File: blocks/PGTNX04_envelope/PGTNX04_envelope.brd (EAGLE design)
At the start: 45.6 x 67.3 mm, 72 parts, among them IC1 TL084P, IC2 AS3310

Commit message: Committed a load of changes
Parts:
- added STN2: HEADER/MALE/01, connectors:HEADER/MALE/01
- moved +V3 26.7 mm to (25.4, 68.6), turned to 270 degrees
- moved GND2 25.7 mm to (22.9, 68.6), turned to 270 degrees
- moved -V3 25.2 mm to (20.3, 68.6), turned to 270 degrees
- moved +V2 23.3 mm to (25.4, 66.0), turned to 270 degrees
- moved GND3 22.2 mm to (22.9, 66.0), turned to 270 degrees
- moved -V2 21.6 mm to (20.3, 66.0), turned to 270 degrees
- moved +V 20.1 mm to (25.4, 63.5), turned to 270 degrees
- moved GND 18.8 mm to (22.9, 63.5), turned to 270 degrees
- moved -V 18.1 mm to (20.3, 63.5), turned to 270 degrees
- moved C1 15.9 mm to (31.8, 64.8), turned to 90 degrees
- moved C2 12.7 mm to (14.0, 64.8)
- moved U$5 9.92 mm to (10.2, 57.1)
- moved U$3 2.54 mm to (3.81, 66.0)
- moved U$4 2.54 mm to (41.9, 66.0)
- moved STN3 2.54 mm to (44.5, 19.1)
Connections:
- new net N$32: STN2.1
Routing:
- net N$8: track 54.2 -> 10.6 mm
- net -12V: track 114.4 -> 82.5 mm, vias 0 -> 1
- net N$20: track 42.3 -> 13.9 mm
- net +12V: track 129.9 -> 151.1 mm
- net N$22: track 22.4 -> 41.7 mm
- net N$30: track 22.7 -> 9.69 mm
- net N$23: track 40.3 -> 27.6 mm
- net N$17: track 47.6 -> 38.4 mm, vias 1 -> 0
- net N$27: track 23.1 -> 15.5 mm
- net N$4: track 20.3 -> 24.8 mm
- net N$10: track 22.0 -> 18.3 mm
- net N$9: track 13.4 -> 11.3 mm
- net N$19: track 11.2 -> 13.2 mm
- net N$21: track 15.1 -> 13.3 mm
- net N$28: track 19.9 -> 18.3 mm
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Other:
- board size 45.6 x 67.3 mm -> 45.6 x 69.8 mm
- board text added: "PGTN020B"
- board text added: "Rob Ellis 2020"

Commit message: Corrected resistor value
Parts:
- R12: value 150R -> 200k
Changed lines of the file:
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@@
 <?xml version="1.0" encoding="utf-8"?>
 <!DOCTYPE eagle SYSTEM "eagle.dtd">
-<eagle version="8.5.2">
+<eagle version="9.6.0">
 <drawing>
 <settings>
-<setting alwaysvectorfont="yes"/>
+<setting alwaysvectorfont="no"/>
 <setting keepoldvectorfont="yes"/>
 <setting verticaltext="up"/>
@@
 <param name="checkStop" value="0"/>
 <param name="checkValues" value="0"/>
+<param name="checkNames" value="1"/>
+<param name="checkWireStubs" value="1"/>
+<param name="checkPolygonWidth" value="0"/>
 <param name="useDiameter" value="13"/>
 <param name="maxErrors" value="50"/>
@@
 <attribute name="SPICEPREFIX" value="X" x="1.27" y="19.05" size="1.778" layer="27" display="off"/>
 </element>
-<element name="R12" library="resistors" package="RESISTOR/7.5" value="150R" x="7.62" y="21.59" smashed="yes">
+<element name="R12" library="resistors" package="RESISTOR/7.5" value="200k" x="7.62" y="21.59" smashed="yes">
 <attribute name="NAME" x="5.08" y="21.082" size="1.016" layer="25" ratio="10"/>
 <attribute name="VALUE" x="4.699" y="22.9362" size="1.27" layer="27" ratio="10"/>
@@
 <attribute name="SPICEPREFIX" value="X" x="44.45" y="19.05" size="1.778" layer="27" rot="R180" display="off"/>
 </element>
-<element name="U$1" library="mechanical" package="STANDOFF/3.0" value="" x="3.81" y="3.81"/>
-<element name="U$2" library="mechanical" package="STANDOFF/3.0" value="" x="41.91" y="3.81"/>
-<element name="U$3" library="mechanical" package="STANDOFF/3.0" value="" x="3.81" y="66.04"/>
-<element name="U$4" library="mechanical" package="STANDOFF/3.0" value="" x="41.91" y="66.04"/>
-<element name="U$5" library="mechanical" package="PIGATRON-LOGO" value="" x="10.16" y="57.15"/>
+<element name="U$1" library="mechanical" package="STANDOFF/3.0" value="" x="3.81" y="3.81" smashed="yes"/>
+<element name="U$2" library="mechanical" package="STANDOFF/3.0" value="" x="41.91" y="3.81" smashed="yes"/>
+<element name="U$3" library="mechanical" package="STANDOFF/3.0" value="" x="3.81" y="66.04" smashed="yes"/>
+<element name="U$4" library="mechanical" package="STANDOFF/3.0" value="" x="41.91" y="66.04" smashed="yes"/>
+<element name="U$5" library="mechanical" package="PIGATRON-LOGO" value="" x="10.16" y="57.15" smashed="yes"/>
 <element name="STN2" library="connectors" package="HEADER/MALE/01" value="HEADER/MALE/01" x="44.45" y="16.51" smashed="yes" rot="R180">
 <attribute name="NAME" x="42.545" y="16.764" size="1.016" layer="25" ratio="10" rot="R180"/>
@@
 </signal>
 </signals>
+<mfgpreviewcolors>
+<mfgpreviewcolor name="soldermaskcolor" color="0xC8008000"/>
+<mfgpreviewcolor name="silkscreencolor" color="0xFFFEFEFE"/>
+<mfgpreviewcolor name="backgroundcolor" color="0xFF282828"/>
+<mfgpreviewcolor name="coppercolor" color="0xFFFFBF00"/>
+<mfgpreviewcolor name="substratecolor" color="0xFF786E46"/>
+</mfgpreviewcolors>
 </board>
 </drawing>

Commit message: Changed resistor value
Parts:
- R1: value 750R -> 470R
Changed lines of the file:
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@@
 <?xml version="1.0" encoding="utf-8"?>
 <!DOCTYPE eagle SYSTEM "eagle.dtd">
-<eagle version="9.6.0">
+<eagle version="9.5.0">
 <drawing>
 <settings>
@@
 <attribute name="VALUE" x="35.179" y="44.704" size="1.27" layer="27" ratio="10" rot="R180"/>
 </element>
-<element name="R1" library="resistors" package="RESISTOR/7.5" value="750R" x="12.7" y="11.43" smashed="yes">
+<element name="R1" library="resistors" package="RESISTOR/7.5" value="470R" x="12.7" y="11.43" smashed="yes">
 <attribute name="NAME" x="10.16" y="10.922" size="1.016" layer="25" ratio="10"/>
 <attribute name="VALUE" x="9.779" y="12.7762" size="1.27" layer="27" ratio="10"/>

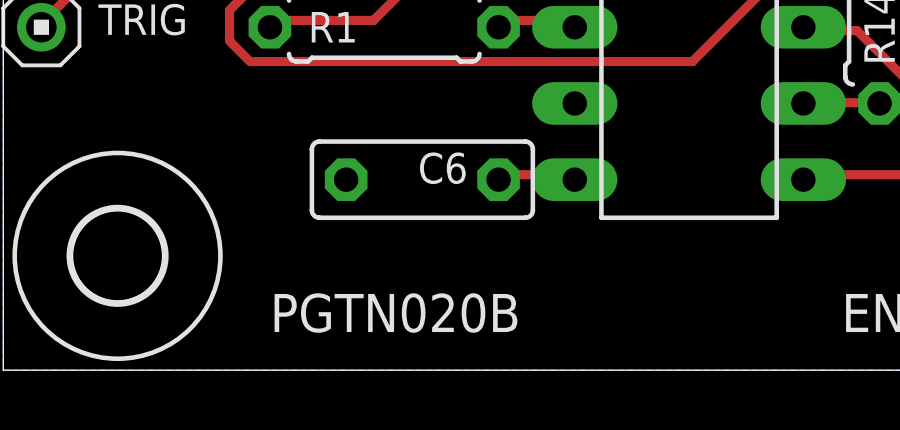
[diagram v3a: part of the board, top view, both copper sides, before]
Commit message: Connected C7 to ground
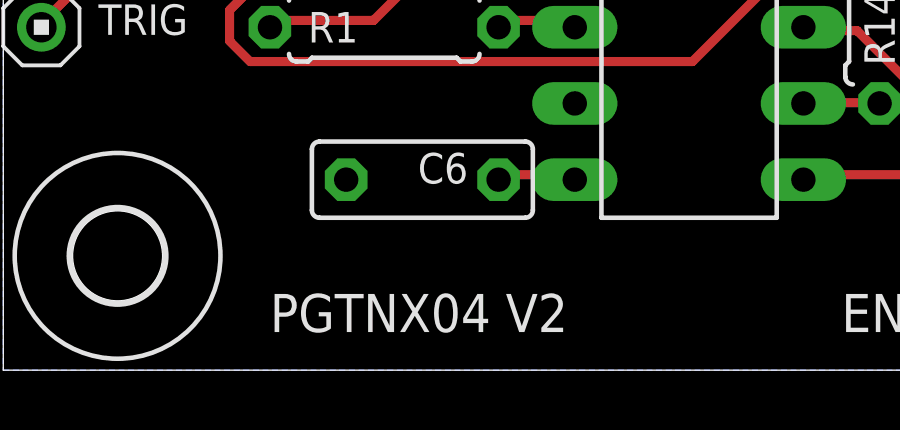
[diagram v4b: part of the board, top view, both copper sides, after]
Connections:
- removed net PE: C7.2
- net GND: now also C7.2
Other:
- board text added: "PGTNX04 V2"
- board text removed: "PGTN020B"
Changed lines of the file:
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@@
 <?xml version="1.0" encoding="utf-8"?>
 <!DOCTYPE eagle SYSTEM "eagle.dtd">
-<eagle version="9.5.0">
+<eagle version="9.6.0">
 <drawing>
 <settings>
@@
 <text x="27.94" y="1.27" size="1.27" layer="25">ENVELOPE</text>
 <dimension x1="0" y1="0" x2="0" y2="69.85" x3="-3.81" y3="34.925" textsize="1.016" layer="51"/>
-<text x="8.89" y="1.27" size="1.27" layer="25">PGTN020B</text>
+<text x="8.89" y="1.27" size="1.27" layer="25">PGTNX04 V2</text>
 <dimension x1="0" y1="0" x2="45.72" y2="0" x3="22.86" y3="-3.81" textsize="1.016" layer="51"/>
 <text x="1.27" y="50.8" size="1.27" layer="25">Rob Ellis 2020</text>
@@
 <contactref element="IC1" pad="10"/>
 <contactref element="IC1" pad="12"/>
+<contactref element="C7" pad="2"/>
 </signal>
 <signal name="+12V">
@@
 <wire x1="18.8595" y1="11.6586" x2="19.05" y2="11.43" width="0.3048" layer="1"/>
 </signal>
-<signal name="PE">
-<contactref element="C7" pad="2"/>
-</signal>
 <signal name="N$13">
